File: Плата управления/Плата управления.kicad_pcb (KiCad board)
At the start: 2 copper layers, 66 x 58.4 mm, 92 parts, among them J1 Conn_01x10, J2 Conn_01x10, J3 Conn_01x02, J4 A, J5 B, J6 C, U1 LMV7239M5, U4 INA283, U5 STM32F071V8Tx

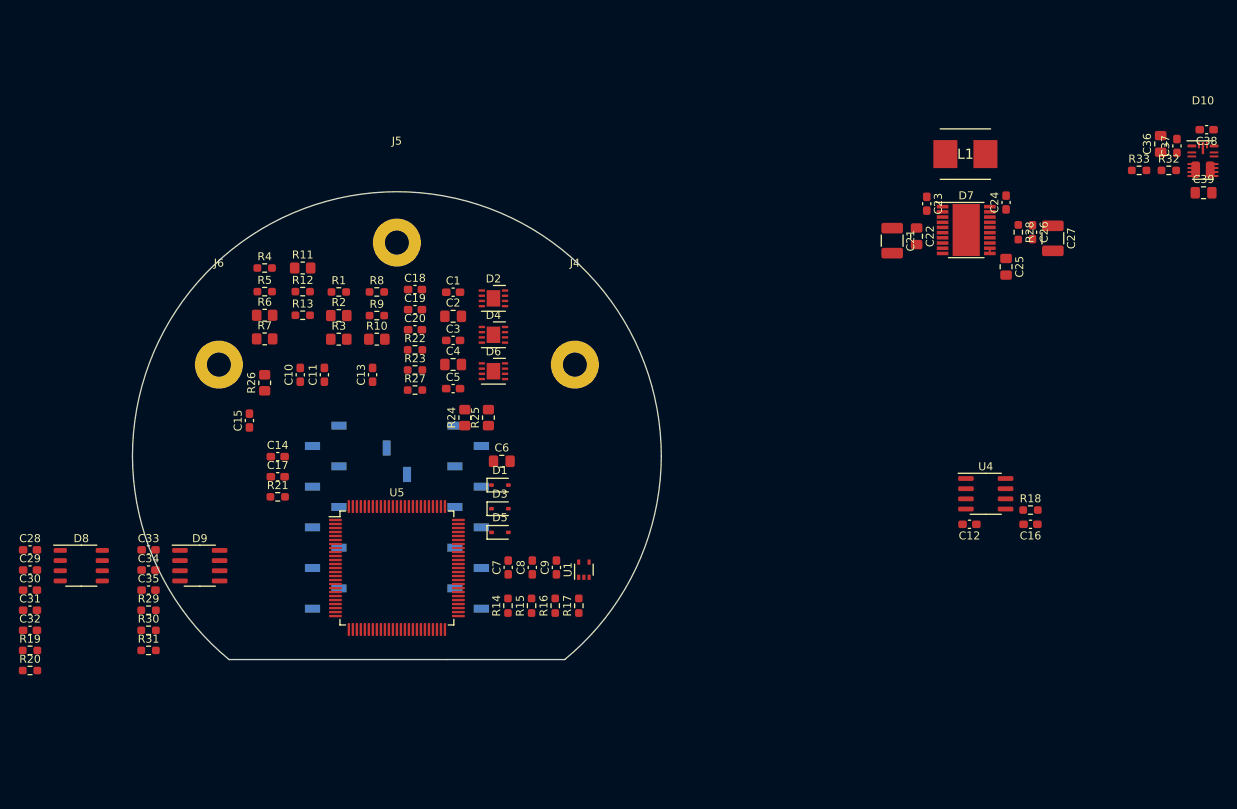
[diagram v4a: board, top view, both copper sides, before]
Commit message: Добавил питание MCU и кварц на 8Мгц
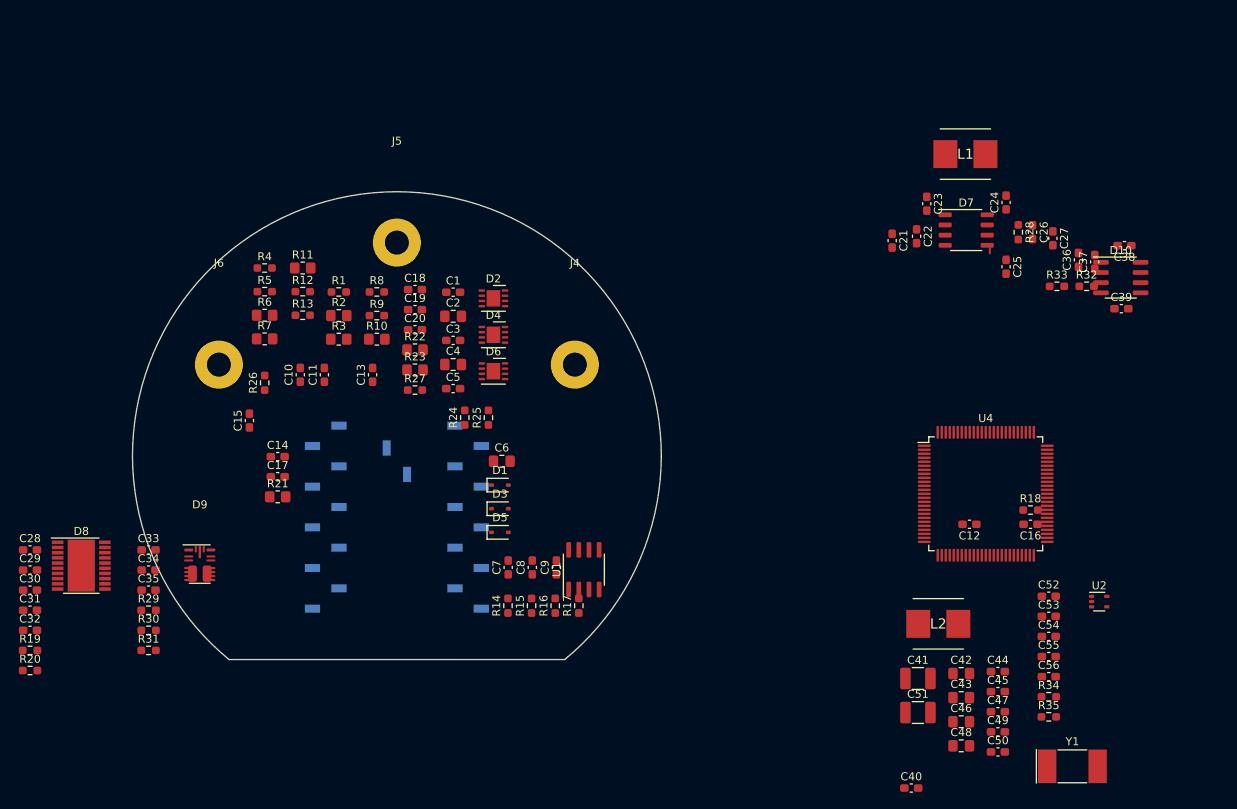
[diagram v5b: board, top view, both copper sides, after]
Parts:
- removed U5: STM32F071V8Tx, Package_QFP:LQFP-100_14x14mm_P0.5mm
- added C40: 100n, Capacitor_SMD:C_0603_1608Metric_Pad1.08x0.95mm_HandSolder, F.Cu at (147.4, 136.1)
- added C41: 10u, Capacitor_SMD:C_1210_3225Metric_Pad1.33x2.70mm_HandSolder, F.Cu at (148.2, 122.4)
- added C42: 470n, Capacitor_SMD:C_0805_2012Metric_Pad1.18x1.45mm_HandSolder, F.Cu at (153.7, 121.8)
- added C43: 4.7u, Capacitor_SMD:C_0805_2012Metric_Pad1.18x1.45mm_HandSolder, F.Cu at (153.7, 124.8)
- added C44: 100n, Capacitor_SMD:C_0603_1608Metric_Pad1.08x0.95mm_HandSolder, F.Cu at (158.2, 121.5)
- added C45: 100n, Capacitor_SMD:C_0603_1608Metric_Pad1.08x0.95mm_HandSolder, F.Cu at (158.2, 124.0)
- added C46: 22u, Capacitor_SMD:C_0805_2012Metric_Pad1.18x1.45mm_HandSolder, F.Cu at (153.7, 127.8)
- added C47: 100n, Capacitor_SMD:C_0603_1608Metric_Pad1.08x0.95mm_HandSolder, F.Cu at (158.2, 126.5)
- added C48: 4.7u, Capacitor_SMD:C_0805_2012Metric_Pad1.18x1.45mm_HandSolder, F.Cu at (153.7, 130.8)
- added C49: 1u, Capacitor_SMD:C_0603_1608Metric_Pad1.08x0.95mm_HandSolder, F.Cu at (158.2, 129.0)
- added C50: 100n, Capacitor_SMD:C_0603_1608Metric_Pad1.08x0.95mm_HandSolder, F.Cu at (158.2, 131.6)
- added C51: 22u, Capacitor_SMD:C_1210_3225Metric_Pad1.33x2.70mm_HandSolder, F.Cu at (148.2, 126.6)
- added C52: 56p, Capacitor_SMD:C_0603_1608Metric_Pad1.08x0.95mm_HandSolder, F.Cu at (164.6, 112.1)
- added C53: 56p, Capacitor_SMD:C_0603_1608Metric_Pad1.08x0.95mm_HandSolder, F.Cu at (164.6, 114.6)
- added C54: 56p, Capacitor_SMD:C_0603_1608Metric_Pad1.08x0.95mm_HandSolder, F.Cu at (164.6, 117.1)
- added C55: 56p, Capacitor_SMD:C_0603_1608Metric_Pad1.08x0.95mm_HandSolder, F.Cu at (164.6, 119.6)
- added C56: 56p, Capacitor_SMD:C_0603_1608Metric_Pad1.08x0.95mm_HandSolder, F.Cu at (164.6, 122.2)
- added L2: 4.7u, Inductor_my:LQH66SN100M03L, F.Cu at (150.8, 115.6)
- added R34: 10k, Resistor_SMD:R_0603_1608Metric_Pad0.98x0.95mm_HandSolder, F.Cu at (164.6, 124.7)
- added R35: 120, Resistor_SMD:R_0603_1608Metric_Pad0.98x0.95mm_HandSolder, F.Cu at (164.6, 127.2)
- added U2: LMV7239M5, Package_TO_SOT_SMD:SOT-353_SC-70-5, F.Cu at (170.9, 112.8)
- added Y1: 8M, Crystal:Crystal_SMD_MicroCrystal_CC1V-T1A-2Pin_8.0x3.7mm, F.Cu at (167.5, 133.3)
- C10, C11, C15: value 100n -> 56p
- C12: value 0.1u -> 100n
- C14, C18, C33, C34, C35: value 56p -> 100n
- C19, C20: value 56p -> 4.3p
- C21: value 10u -> 100n; footprint Capacitor_SMD:C_1210_3225Metric_Pad1.33x2.70mm_HandSolder -> Capacitor_SMD:C_0603_1608Metric_Pad1.08x0.95mm_HandSolder
- C22: value 470n -> 100n; footprint Capacitor_SMD:C_0805_2012Metric_Pad1.18x1.45mm_HandSolder -> Capacitor_SMD:C_0603_1608Metric_Pad1.08x0.95mm_HandSolder
- C24: value 100n -> 4.7u
- C25: value 4.7u -> 1u; footprint Capacitor_SMD:C_0805_2012Metric_Pad1.18x1.45mm_HandSolder -> Capacitor_SMD:C_0603_1608Metric_Pad1.08x0.95mm_HandSolder
- C27: value 22u -> 100n; footprint Capacitor_SMD:C_1210_3225Metric_Pad1.33x2.70mm_HandSolder -> Capacitor_SMD:C_0603_1608Metric_Pad1.08x0.95mm_HandSolder
- C29, C30: value 1n -> 100n
- C36: value 4.7u -> 1n; footprint Capacitor_SMD:C_0805_2012Metric_Pad1.18x1.45mm_HandSolder -> Capacitor_SMD:C_0603_1608Metric_Pad1.08x0.95mm_HandSolder
- C37: value 100n -> 1n
- C38: value 1u -> 100n
- C39: value 22u -> 100n; footprint Capacitor_SMD:C_0805_2012Metric_Pad1.18x1.45mm_HandSolder -> Capacitor_SMD:C_0603_1608Metric_Pad1.08x0.95mm_HandSolder
- C7, C9: value 56p -> 0.1u
- C8: value 0.1u -> 56p
- D10: value TPSM33625 -> SIT65HVD232DR; footprint Convertor_DCDC_My:QFN-FCMOD -> Package_SO:SOIC-8_3.9x4.9mm_P1.27mm
- D7: value TPS55165QPWPRQ1 -> NSM3012; footprint Package_SO:HTSSOP-20-1EP_4.4x6.5mm_P0.65mm_EP3.4x6.5mm -> Package_SO:SOP-8_3.9x4.9mm_P1.27mm
- D8: value NSM3012 -> TPS55165QPWPRQ1; footprint Package_SO:SOP-8_3.9x4.9mm_P1.27mm -> Package_SO:HTSSOP-20-1EP_4.4x6.5mm_P0.65mm_EP3.4x6.5mm
- D9: value SIT65HVD232DR -> TPSM33625; footprint Package_SO:SOIC-8_3.9x4.9mm_P1.27mm -> Convertor_DCDC_My:QFN-FCMOD
- R15: value 1k -> 1.6k
- R17, R18: value 120 -> 1k
- R19: value 10 -> 120
- R20: value 50 -> 120
- R21, R22, R23: value 120 -> 10k; footprint Resistor_SMD:R_0603_1608Metric_Pad0.98x0.95mm_HandSolder -> Resistor_SMD:R_0805_2012Metric_Pad1.20x1.40mm_HandSolder
- R24, R25, R26: value 10k -> 120; footprint Resistor_SMD:R_0805_2012Metric_Pad1.20x1.40mm_HandSolder -> Resistor_SMD:R_0603_1608Metric_Pad0.98x0.95mm_HandSolder
- R27: value 120 -> 10
- R28: value 100k -> 50
- R29, R30, R31: value 10k -> 100k
- R32, R33: value 100k -> 10k
- U1: value LMV7239M5 -> AD8210; footprint Package_TO_SOT_SMD:SOT-353_SC-70-5 -> Package_SO:SOIC-8_3.9x4.9mm_P1.27mm
- U4: value INA283 -> STM32F767VITx; footprint Package_SO:SOIC-8_3.9x4.9mm_P1.27mm -> Package_QFP:LQFP-100_14x14mm_P0.5mm
- moved C36 17.7 mm to (168.3, 70.1)
- moved C38 17.7 mm to (174.0, 68.3)
- moved R32 17.7 mm to (169.3, 73.4)
- moved R33 17.7 mm to (165.6, 73.4)
- moved C37 17.7 mm to (170.3, 70.4)
- moved C39 17.7 mm to (173.7, 76.2)
- moved D10 17.7 mm to (173.6, 72.3)
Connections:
- C10 pad 1: GND -> Enable
- C10 pad 2: +3.3V -> GND
- C11 pad 1: GND -> DC_Current_MCU
- C11 pad 2: Temp_B -> GND
- C12 pad 1: +3.3V -> GND
- C12 pad 2: GND -> Temp_A
- C13 pad 2: Temp_A -> Temp_B
- C14 pad 2: Net-(D9-D) -> Temp_C
- C15 pad 1: GND -> Temp_A_MCU
- C15 pad 2: Temp_C -> GND
- C16 pad 1: DC_Current_MCU -> Temp_B_MCU
- C17 pad 1: GND -> Temp_C_MCU
- C17 pad 2: CANH -> GND
- C18 pad 1: Temp_A_MCU -> GND
- C18 pad 2: GND -> +3.3V
- C19 pad 1: Temp_B_MCU -> GND
- C19 pad 2: GND -> Net-(U4-PH0)
- C20 pad 1: Temp_C_MCU -> GND
- C20 pad 2: GND -> Net-(U4-PH1)
- C21 pad 1: +24V -> VDD
- C22 pad 1: +24V -> VDD
- C23 pad 1: Net-(D7-L1) -> VDD
- C23 pad 2: Net-(D7-BST1) -> GND
- C24 pad 1: Net-(D7-BST2) -> VDD
- C24 pad 2: Net-(D7-L2) -> GND
- C25 pad 1: Net-(D7-VOS_FB) -> VDD
- C26 pad 1: +12V -> VDD
- C27 pad 1: +12V -> VDD
- C28 pad 1: Net-(D8-VDD) -> VDD
- C29 pad 1: +3.3V -> VDD
- C30 pad 1: GND -> VDD
- C30 pad 2: Net-(C30-Pad2) -> GND
- C31 pad 1: GND -> VDD
- C31 pad 2: Net-(D8-OUT) -> GND
- C32 pad 1: GND -> VDDA
- C32 pad 2: Net-(D8-VLDO) -> GND
- C33 pad 1: GND -> VDD
- C33 pad 2: +3.3V -> GND
- C34 pad 1: GND -> VDD
- C34 pad 2: +3.3V -> GND
- C35 pad 1: CANL -> VDD
- C36 pad 1: +12V -> +3.3V
- C37 pad 1: +12V -> GND
- C37 pad 2: GND -> Net-(C37-Pad2)
- C38 pad 1: Net-(D10-VCC) -> Net-(D7-VDD)
- C39 pad 1: +3.3V -> GND
- C39 pad 2: GND -> Net-(D7-OUT)
- C7 pad 1: Net-(U1--) -> GND
- C7 pad 2: GND -> +5V
- C8 pad 1: +3.3V -> Net-(U2--)
- C9 pad 1: Enable -> +3.3V
- D10 pad 1: unconnected-(D10-PGOOD-Pad1) -> Net-(D10-D)
- D10 pad 2: +12V -> GND
- D10 pad 3: +12V -> +3.3V
- D10 pad 4: +3.3V -> Net-(D10-R)
- D10 pad 5: Net-(D10-SW-Pad5) -> unconnected-(D10-NC-Pad5)
- D10 pad 6: Net-(D10-SW-Pad5) -> CANL
- D10 pad 7: unconnected-(D10-BOOT-Pad7) -> CANH
- D10 pad 8: Net-(D10-VCC) -> unconnected-(D10-NC-Pad8)
- D7 pad 1: GND -> Net-(D7-VDD)
- D7 pad 2: Net-(D7-L1) -> unconnected-(D7-NC-Pad2)
- D7 pad 3: Net-(D7-BST1) -> Net-(D7-OUT)
- D7 pad 4: +24V -> SCLK_MCU
- D7 pad 5: +24V -> CS_MCU
- D7 pad 6: +24V -> SDIO_MCU
- D7 pad 7: unconnected-(D7-PS-Pad7) -> Net-(D7-VLDO)
- D8 pad 1: Net-(D8-VDD) -> GND
- D8 pad 2: unconnected-(D8-NC-Pad2) -> Net-(D8-L1)
- D8 pad 3: Net-(D8-OUT) -> Net-(D8-BST1)
- D8 pad 4: SCLK_MCU -> +24V
- D8 pad 5: CS_MCU -> +24V
- D8 pad 6: SDIO_MCU -> +24V
- D8 pad 7: Net-(D8-VLDO) -> unconnected-(D8-PS-Pad7)
- D9 pad 1: Net-(D9-D) -> unconnected-(D9-PGOOD-Pad1)
- D9 pad 2: GND -> +12V
- D9 pad 3: +3.3V -> +12V
- D9 pad 4: Net-(D9-R) -> +3.3V
- D9 pad 5: unconnected-(D9-NC-Pad5) -> Net-(D9-SW-Pad5)
- D9 pad 6: CANL -> Net-(D9-SW-Pad5)
- D9 pad 7: CANH -> unconnected-(D9-BOOT-Pad7)
- D9 pad 8: unconnected-(D9-NC-Pad8) -> Net-(D9-VCC)
- R14 pad 1: Net-(U1-+) -> Net-(U1-OUT)
- R14 pad 2: GND -> Net-(R14-Pad2)
- R15 pad 1: +3.3V -> GND
- R15 pad 2: Net-(U1-+) -> Net-(R14-Pad2)
- R16 pad 1: Net-(U1--) -> Net-(U2--)
- R16 pad 2: DC_Current_MCU -> Net-(R14-Pad2)
- R17 pad 1: Net-(R17-Pad1) -> +5V
- R17 pad 2: Enable -> Net-(U2-+)
- R18 pad 1: Net-(R18-Pad1) -> Net-(U2-+)
- R18 pad 2: DC_Current_MCU -> GND
- R19 pad 1: +3.3V -> Net-(R19-Pad1)
- R19 pad 2: Net-(D8-VDD) -> Enable
- R20 pad 1: Net-(C30-Pad2) -> Net-(U3D--)
- R20 pad 2: Net-(D8-OUT) -> DC_Current_MCU
- R21 pad 1: CANL -> +3.3V
- R21 pad 2: CANH -> Temp_A
- R22 pad 1: Net-(U8A--) -> +3.3V
- R22 pad 2: Temp_A_MCU -> Temp_B
- R23 pad 1: Net-(U8B--) -> +3.3V
- R23 pad 2: Temp_B_MCU -> Temp_C
- R24 pad 1: +3.3V -> Net-(U3A--)
- R24 pad 2: Temp_A -> Temp_A_MCU
- R25 pad 1: +3.3V -> Net-(U3B--)
- R25 pad 2: Temp_B -> Temp_B_MCU
- R26 pad 1: +3.3V -> Net-(U3C--)
- R26 pad 2: Temp_C -> Temp_C_MCU
- R27 pad 1: Net-(U8C--) -> +3.3V
- R27 pad 2: Temp_C_MCU -> Net-(D7-VDD)
- R28 pad 1: +12V -> Net-(C37-Pad2)
- R28 pad 2: Net-(D7-PG) -> Net-(D7-OUT)
- R29 pad 1: Net-(D9-D) -> Net-(D9-FB)
- R29 pad 2: CAN_TXD -> +3.3V
- R30 pad 1: Net-(D9-D) -> GND
- R30 pad 2: +3.3V -> Net-(D9-FB)
- R31 pad 1: Net-(D9-R) -> +12V
- R31 pad 2: CAN_RXD -> Net-(D8-PG)
- R32 pad 1: Net-(D10-FB) -> Net-(D10-D)
- R32 pad 2: +3.3V -> CAN_TXD
- R33 pad 1: GND -> Net-(D10-R)
- R33 pad 2: Net-(D10-FB) -> CAN_RXD
- U1 pad 1: Net-(R17-Pad1) -> Shunt_2
- U1 pad 3: Net-(U1-+) -> GND
- U1 pad 4: Net-(U1--) -> unconnected-(U1-NC-Pad4)
- U1 pad 5: +3.3V -> Net-(U1-OUT)
- U4 pad 1: Shunt_2 -> unconnected-(U4-PE2-Pad1)
- U4 pad 2: GND -> unconnected-(U4-PE3-Pad2)
- U4 pad 3: +3.3V -> unconnected-(U4-PE4-Pad3)
- U4 pad 5: Net-(R18-Pad1) -> unconnected-(U4-PE6-Pad5)
- U4 pad 6: +3.3V -> VDD
- U4 pad 7: GND -> unconnected-(U4-PC13-Pad7)
- U4 pad 8: Shunt_1 -> unconnected-(U4-PC14-Pad8)
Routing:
- net Net-(D7-VOS_FB): track 1.01 -> 0.00 mm
- net VDD: track 0.00 -> 0.80 mm
- net CS_MCU: track 0.00 -> 0.65 mm

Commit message: Расставил драйвера
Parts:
- removed C11: 56p, Capacitor_SMD:C_0603_1608Metric_Pad1.08x0.95mm_HandSolder
- removed R14: 1k, Resistor_SMD:R_0603_1608Metric_Pad0.98x0.95mm_HandSolder
- removed R15: 1.6k, Resistor_SMD:R_0603_1608Metric_Pad0.98x0.95mm_HandSolder
- removed R20: 120, Resistor_SMD:R_0603_1608Metric_Pad0.98x0.95mm_HandSolder
- removed U1: AD8210, Package_SO:SOIC-8_3.9x4.9mm_P1.27mm
- added U5: INA283, Package_SO:SOIC-8_3.9x4.9mm_P1.27mm, F.Cu at (129.1, 96.9)
- C1, C2, C23, C24, C25, C3, C31, C32, C35, C4, C5, C6, D1, D2, D3, D4, D5, D6, R1, R10, R11, R12, R13, R2, R3, R4, R5, R6, R7, R8, R9: moved to B.Cu
- moved D9 120.6 mm to (173.7, 72.4)
- moved D8 118.7 mm to (154.3, 64.9)
- moved Y1 102.1 mm to (68.7, 107.6), turned to 90 degrees
- moved C27 91.5 mm to (82.8, 107.4)
- moved C25 85.0 mm to (75.4, 85.3), turned to 90 degrees
- moved C26 84.4 mm to (88.6, 107.4)
- moved C21 78.6 mm to (77.2, 107.4)
- moved C23 78.5 mm to (84.6, 107.4)
- moved U4 74.0 mm to (82.8, 96.5)
- moved C22 73.2 mm to (77.2, 85.3), turned to 90 degrees
- moved C24 72.6 mm to (90.2, 85.3), turned to -90 degrees
- moved C30 57.3 mm to (88.4, 85.3), turned to 90 degrees
- moved R24 54.1 mm to (115.8, 41.4)
- moved C14 53.7 mm to (95.0, 48.0)
- moved C15 53.7 mm to (91.4, 43.5)
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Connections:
- C21 pad 1: VDD -> +3.3V
- C22 pad 1: VDD -> +3.3V
- C23 pad 1: VDD -> +3.3V
- C24 pad 1: VDD -> +3.3V
- C25 pad 1: VDD -> +3.3V
- C26 pad 1: VDD -> +3.3V
- C27 pad 1: VDD -> +3.3V
- C28 pad 1: VDD -> +3.3V
- C29 pad 1: VDD -> +3.3V
- C30 pad 1: VDD -> +3.3V
- C31 pad 1: VDD -> +3.3V
- C33 pad 1: VDD -> +3.3V
- C34 pad 1: VDD -> +3.3V
- C35 pad 1: VDD -> +3.3V
- C7 pad 1: GND -> +3.3V
- C7 pad 2: +5V -> GND
- J1 pad 1: B -> Temp_B
- J1 pad 10: Shunt_1 -> G5
- J1 pad 2: G3 -> GND
- J1 pad 3: G2 -> GND
- J1 pad 4: GND -> G4
- J1 pad 5: Temp_A -> GND
- J1 pad 6: GND -> G6
- J1 pad 7: G1 -> Temp_C
- J1 pad 8: A -> GND
- J1 pad 9: Shunt_2 -> C
- J2 pad 1: unconnected-(J2-Pin_1-Pad1) -> B
- J2 pad 10: unconnected-(J2-Pin_10-Pad10) -> Shunt_1
- J2 pad 2: unconnected-(J2-Pin_2-Pad2) -> G3
- J2 pad 3: unconnected-(J2-Pin_3-Pad3) -> G2
- J2 pad 4: unconnected-(J2-Pin_4-Pad4) -> GND
- J2 pad 5: unconnected-(J2-Pin_5-Pad5) -> Temp_A
- J2 pad 6: unconnected-(J2-Pin_6-Pad6) -> GND
- J2 pad 7: unconnected-(J2-Pin_7-Pad7) -> G1
- J2 pad 8: unconnected-(J2-Pin_8-Pad8) -> A
- J2 pad 9: unconnected-(J2-Pin_9-Pad9) -> Shunt_2
- R17 pad 1: +5V -> +3.3V
- U4 pad 100: unconnected-(U4-VDD-Pad100) -> +3.3V
- U4 pad 11: VDD -> +3.3V
- U4 pad 21: VDD -> +3.3V
- U4 pad 27: VDD -> +3.3V
- U4 pad 50: VDD -> +3.3V
- U4 pad 6: VDD -> +3.3V
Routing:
- net VDD: track 0.80 -> 0.00 mm
- net +3.3V: track 0.00 -> 0.80 mm
- net CS_MCU: track 0.65 -> 0.00 mm

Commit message: Добавил EEPROM
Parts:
- removed C36, C37: 1n, Capacitor_SMD:C_0603_1608Metric_Pad1.08x0.95mm_HandSolder
- removed C38, C39, C40: 100n, Capacitor_SMD:C_0603_1608Metric_Pad1.08x0.95mm_HandSolder
- removed D7: NSM3012, Package_SO:SOP-8_3.9x4.9mm_P1.27mm
- removed R27: 10, Resistor_SMD:R_0603_1608Metric_Pad0.98x0.95mm_HandSolder
- removed R28: 50, Resistor_SMD:R_0603_1608Metric_Pad0.98x0.95mm_HandSolder
- added C11: 1u, Capacitor_SMD:C_0603_1608Metric_Pad1.08x0.95mm_HandSolder, F.Cu at (122.7, 124.7)
- added U1: AT25xxx, Package_SO:SOIC-8_3.9x4.9mm_P1.27mm, F.Cu at (124.8, 120.3)
- Y1: footprint Crystal:Crystal_SMD_MicroCrystal_CC1V-T1A-2Pin_8.0x3.7mm -> Crystal:Crystal_SMD_HC49-SD

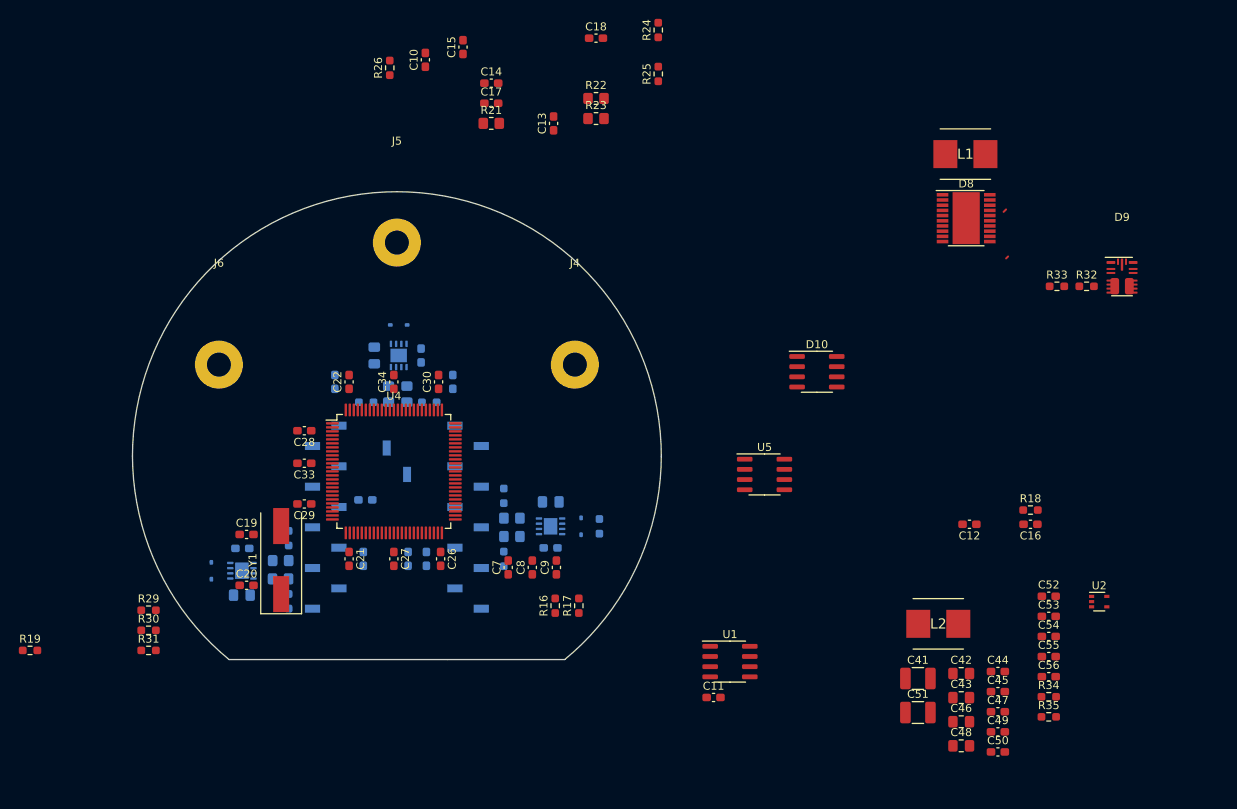
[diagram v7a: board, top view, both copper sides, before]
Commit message: Расставил компоненты по плате
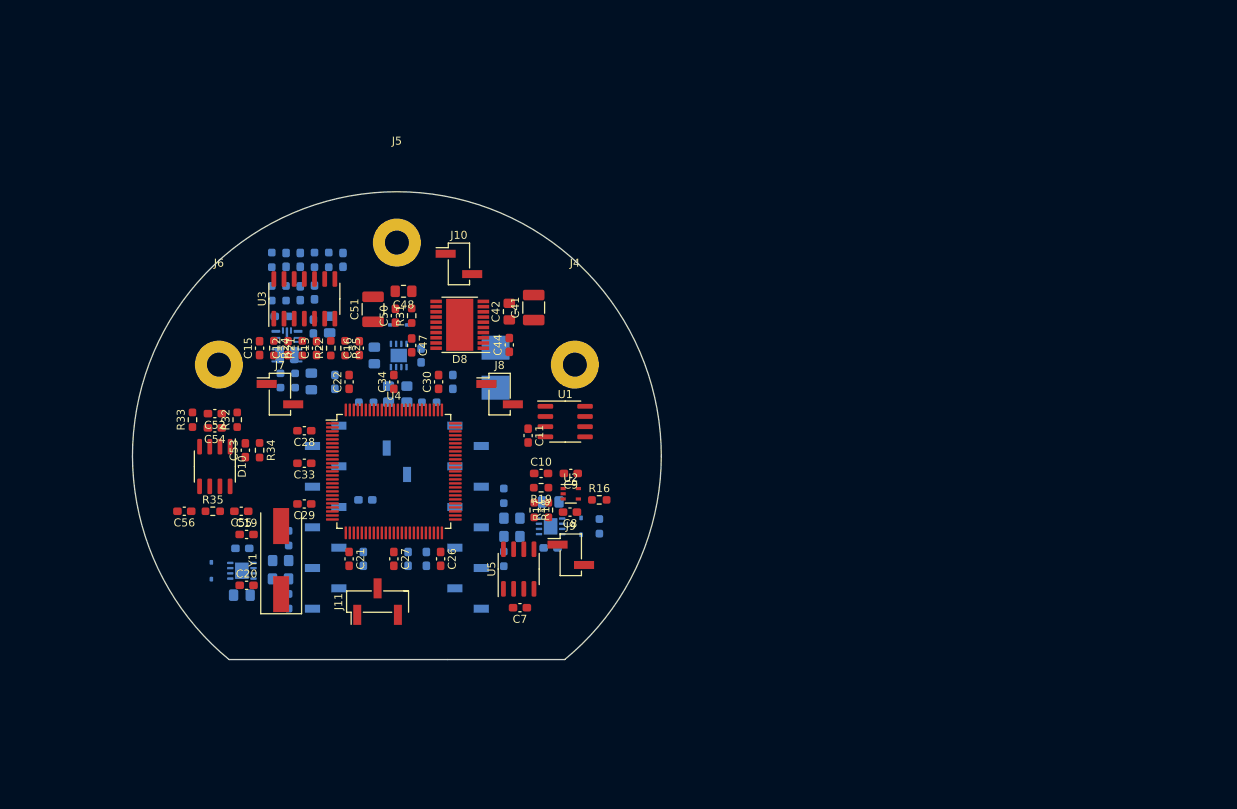
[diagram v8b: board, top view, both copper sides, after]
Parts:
- removed L1: 4.7u, Inductor_my:LQH66SN100M03L
- added C36: 100n, Capacitor_SMD:C_0603_1608Metric_Pad1.08x0.95mm_HandSolder, B.Cu at (71.1, 74.3)
- added C37: 56p, Capacitor_SMD:C_0603_1608Metric_Pad1.08x0.95mm_HandSolder, B.Cu at (76.5, 70.1)
- added J10: Conn_01x02, Connector_PinHeader_2.54mm:PinHeader_1x02_P2.54mm_Vertical_SMD_Pin1Left, F.Cu at (90.9, 70.6)
- added J11: Conn_01x03, Connector_PinHeader_2.54mm:PinHeader_1x03_P2.54mm_Vertical_SMD_Pin1Left, F.Cu at (80.8, 112.8)
- added J7: Conn_01x02, Connector_PinHeader_2.54mm:PinHeader_1x02_P2.54mm_Vertical_SMD_Pin1Left, F.Cu at (68.6, 86.9)
- added J8: Conn_01x02, Connector_PinHeader_2.54mm:PinHeader_1x02_P2.54mm_Vertical_SMD_Pin1Left, F.Cu at (96.0, 86.9)
- added J9: Conn_01x02, Connector_PinHeader_2.54mm:PinHeader_1x02_P2.54mm_Vertical_SMD_Pin1Left, F.Cu at (104.9, 106.9)
- added R14: 10k, Resistor_SMD:R_0603_1608Metric_Pad0.98x0.95mm_HandSolder, B.Cu at (67.6, 74.3)
- added R15: 10k, Resistor_SMD:R_0603_1608Metric_Pad0.98x0.95mm_HandSolder, B.Cu at (69.3, 74.3)
- added R20: 120, Resistor_SMD:R_0603_1608Metric_Pad0.98x0.95mm_HandSolder, B.Cu at (74.7, 70.1)
- added U3: LMV324, Package_SO:SOIC-14_3.9x8.7mm_P1.27mm, F.Cu at (71.6, 75.0)
- C14, C17, C18, C43, C45, C46, C49, D9, L2, R26, R29, R30: moved to B.Cu
- R21, R22: footprint Resistor_SMD:R_0805_2012Metric_Pad1.20x1.40mm_HandSolder -> Resistor_SMD:R_0603_1608Metric_Pad0.98x0.95mm_HandSolder
- R23: footprint Resistor_SMD:R_0805_2012Metric_Pad1.20x1.40mm_HandSolder -> Resistor_SMD:R_0603_1608Metric_Pad0.98x0.95mm_HandSolder; moved to B.Cu
- moved C56 109.9 mm to (56.6, 101.5), turned to 180 degrees
- moved R33 109.2 mm to (57.7, 90.1), turned to 90 degrees
- moved R35 107.5 mm to (60.2, 101.5)
- moved R32 107.4 mm to (63.2, 90.1), turned to 90 degrees
- moved C54 107.3 mm to (60.5, 91.1), turned to 180 degrees
- moved C52 106.6 mm to (60.5, 89.3), turned to 180 degrees
- moved D9 104.6 mm to (69.5, 81.0), turned to 180 degrees
- moved C49 103.4 mm to (68.8, 77.2)
- moved R34 103.2 mm to (66.0, 93.9), turned to -90 degrees
- moved C55 102.5 mm to (63.8, 101.5), turned to 180 degrees
- moved C53 102.4 mm to (64.3, 93.9), turned to 90 degrees
- moved C45 96.9 mm to (72.8, 78.4), turned to 90 degrees
- moved C50 92.9 mm to (83.0, 77.1), turned to 90 degrees
- moved C46 91.6 mm to (72.5, 85.3), turned to -90 degrees
- moved C43 91.6 mm to (74.8, 78.2), turned to 90 degrees
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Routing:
- net +3.3V: track 0.80 -> 0.00 mm
